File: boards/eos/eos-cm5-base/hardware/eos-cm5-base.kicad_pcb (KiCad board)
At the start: 4 copper layers, 90 x 80 mm, 36 parts, among them J1 CM5 1-100, J2 CM5 101-200, J3 USB-C, J4 USB-A, J5 TRJG0926HENL, J6 microSD, J7 GPIO, J8 FAN, J9 BOOT, SW1 POWER, U1 USBLC6-2SC6, U2 TPS2051C, U3 USBLC6-2SC6, U4 TPD4EUSB30, U5 TPD4EUSB30, U6 RT9742GGJ5

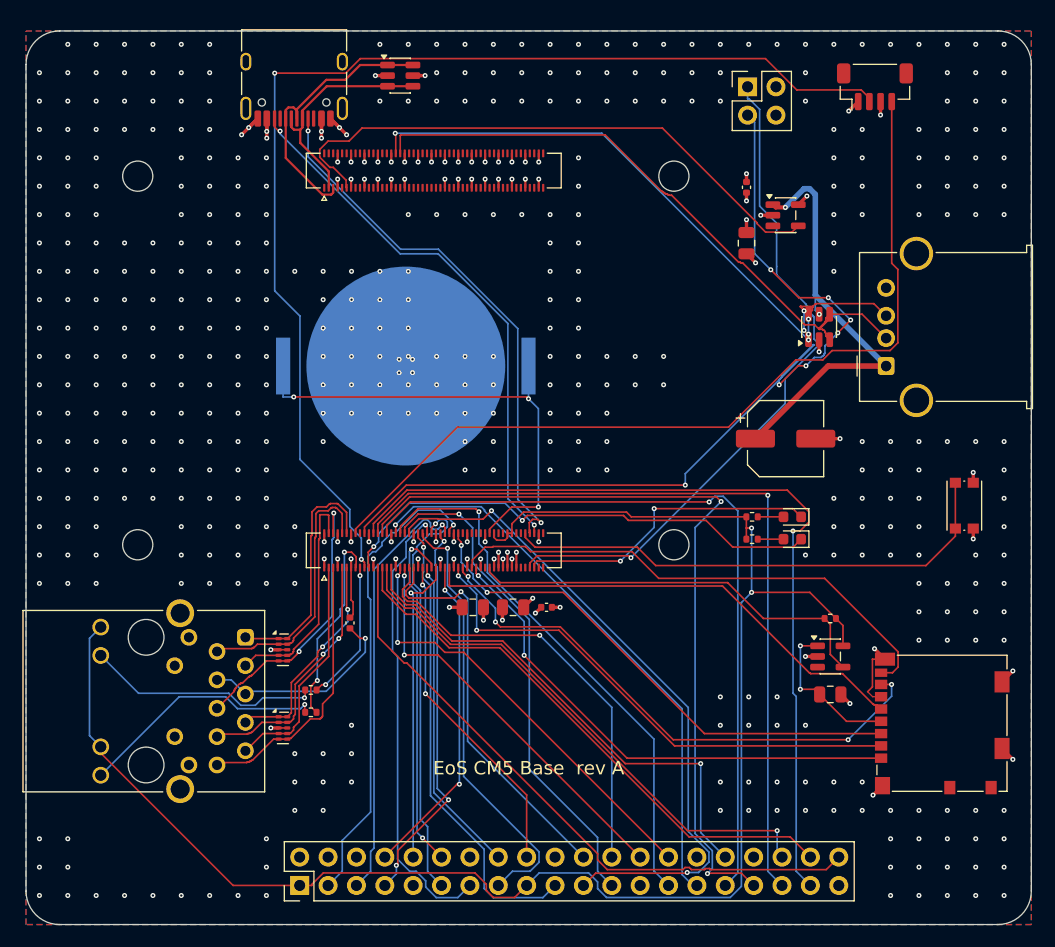
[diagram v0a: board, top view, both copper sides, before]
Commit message: fix(boards): no copper under the CM5's antenna on EoS CM5 Base
The CM5 datasheet (section 4.1.2) says "Don't place any metal, including ground planes,
directly beneath the antenna" and asks for a ground-plane cut-out of at least 6.5 x 11 mm,
ideally 8 x 15 mm. EoS CM5 Base had its ground and 5 V planes and both pours under the whole
module, the antenna included.

- tools/eos_boards gains `copper_keepouts`: rectangles kept free of copper on every layer.
  Each is a rule area on the saved board (no tracks, vias, pads or pours), so zone fills, the
  router's DSN and DRC all honour it. _inside() also refuses them, so the plane fan-out, the
  ground stitching and the maze router never put a via or track there.
- EoS CM5 Base keeps the datasheet's ideal 8 x 15 mm clear where Figure 4 puts the cut-out:
  the module's pin-99 edge, 18.5 mm up from the pin-200 edge. That is x 55-63, y 26-41 mm on
  the board, and nothing is placed there.
- With the planes cut back there, the autorouter boxed SD_DAT0 in and the build stopped at 1
  unconnected item. So SD_DAT1, SD_DAT0 and SD_CLK are now routed first, shortest first, and
  nest on the top layer. Rebuilt: ERC 0, DRC errors 0, unconnected 0, parity 0, 6 silkscreen
  warnings as before.
- AntennaKeepoutTest reads the built board and checks four things:
  - the rule area is there, on every copper layer;
  - it covers Figure 4's cut-out and is at least 8 x 15 mm;
  - no track or via enters it;
  - no pour covers any of 49 points inside it.
  It fails on the previous board (no rule area). It also fails on this board with one track or
  one via added inside, and KiCad's DRC then reports items_not_allowed too.
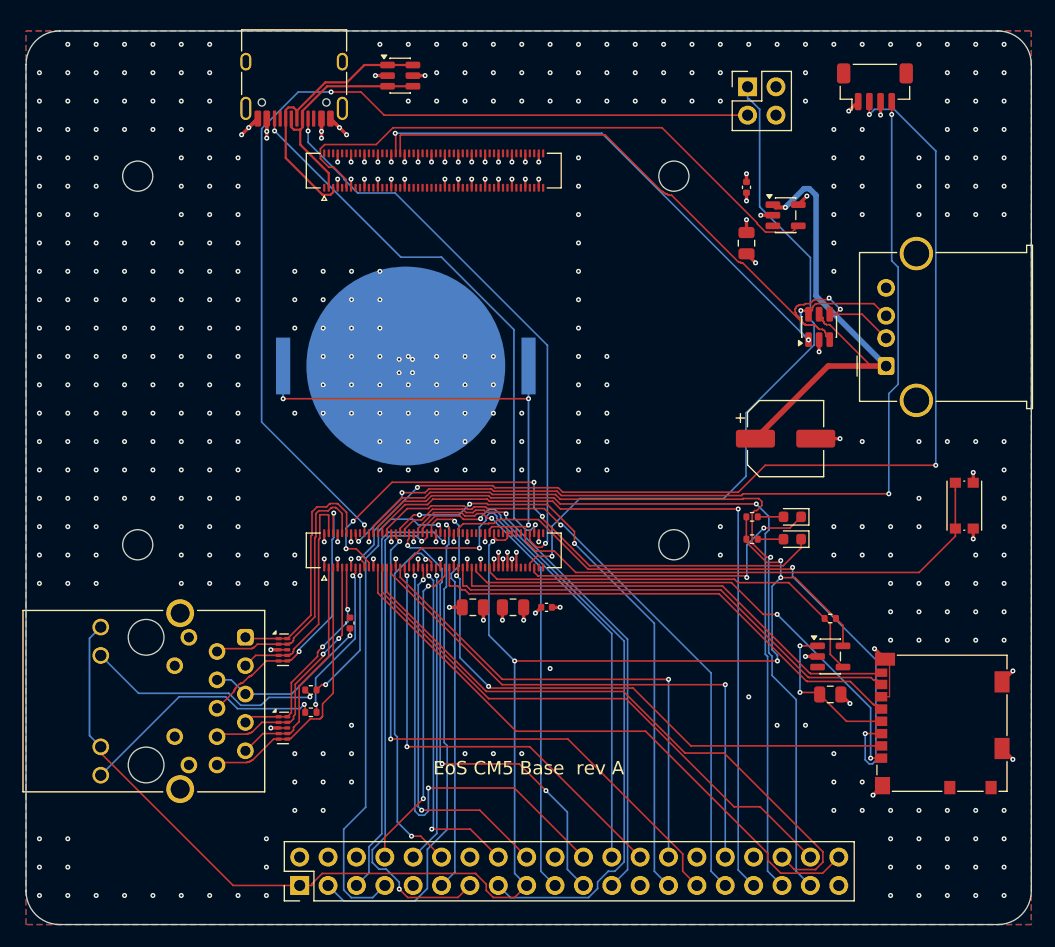
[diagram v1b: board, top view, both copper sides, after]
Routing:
- net /GPIO22: track 39.0 -> 57.7 mm
- net /GPIO9: track 60.1 -> 42.9 mm, vias 2 -> 3
- net /GPIO6: track 67.7 -> 56.2 mm
- net /SD_CMD: track 46.9 -> 57.9 mm
- net /GPIO4: track 34.9 -> 44.7 mm, vias 3 -> 1
- net +3V3: track 149.9 -> 141.0 mm, vias 2 -> 5
- net /FAN_TACHO: track 77.6 -> 86.5 mm, vias 0 -> 4
- net /FAN_PWM: track 103.1 -> 94.4 mm, vias 2 -> 4
- net /LED_NACT: track 44.7 -> 53.3 mm, vias 2 -> 4
- net /GPIO16: track 48.4 -> 56.2 mm, vias 1 -> 0
- net /GPIO8: track 39.1 -> 46.4 mm
- net /SD_DAT0: track 49.6 -> 42.7 mm, vias 4 -> 0
- net /USBH_VBUS: track 39.0 -> 45.3 mm, vias 2 -> 1
- net /USBH_DM: track 56.9 -> 63.1 mm, vias 0 -> 2
- net GND: track 80.9 -> 75.2 mm, vias 499 -> 460
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
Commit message: fix(boards): USB-C receptacles at HRO's recommended edge distance
Each HRO TYPE-C-31-M-12 now sits with its footprint origin 3.19 mm from the
board edge it faces (design.USB_C_EDGE). HRO's "RECOMMEND P.C.B LAYOUT" draws
the PCB edge 5.79 mm from the locating pegs, which are 2.60 mm behind the
origin. At the old 3.8 mm the shell's face was 0.15 mm behind the edge, so a
plug's overmold could meet the board before the plug seated; the shell now
stands about 0.46 mm proud of it.

EoS Learn RP2350, EoS Probe S3 and EoS CM5 Base are moved and rebuilt: all
three report ERC 0, DRC errors 0, unconnected 0, schematic parity 0, with the
same DRC warnings as before (4, 4 and 6). On EoS CM5 Base, GPIO2 (the
header's SDA, CM5 pin 58) is now a priority route: after the move the
autorouter boxed its pad in twice, also with 100 passes.

UsbCEdgeTest checks every board's receptacles against the constant, within
the drawing's 0.05 mm tolerance. It fails for the old 3.8 mm placement.

Found in the independent review of a later board (EoS TM4C123 Board, M1).
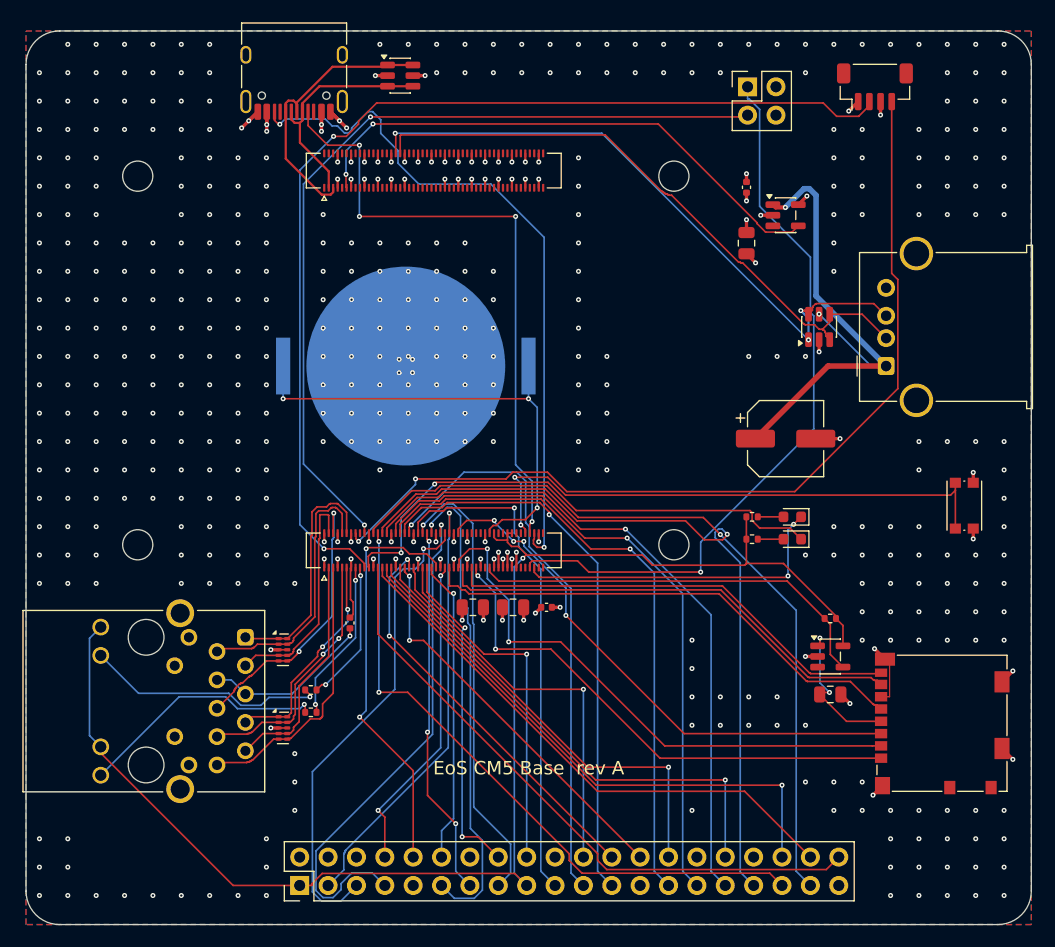
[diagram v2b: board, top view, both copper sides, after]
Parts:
- moved J3 0.61 mm to (24.0, 3.19)
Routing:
- net /GPIO22: track 57.7 -> 41.0 mm
- net /GPIO19: track 71.3 -> 57.9 mm, vias 1 -> 2
- net /CC2: track 50.1 -> 62.5 mm
- net +3V3: track 141.0 -> 128.9 mm, vias 5 -> 1
- net /GPIO27: track 44.8 -> 33.2 mm, vias 2 -> 3
- net /GPIO15: track 26.8 -> 37.1 mm, vias 1 -> 2
- net /GPIO8: track 46.4 -> 36.4 mm, vias 1 -> 2
- net /EEPROM_NWP: track 85.8 -> 75.8 mm
- net /SD_CMD: track 57.9 -> 48.2 mm, vias 2 -> 4
- net /GPIO9: track 42.9 -> 51.7 mm, vias 3 -> 1
- net /USBH_DM: track 63.1 -> 55.5 mm, vias 2 -> 0
- net /LED_NACT: track 53.3 -> 46.9 mm, vias 4 -> 2
- net /GPIO17: track 36.8 -> 43.2 mm
- net /GPIO25: track 41.9 -> 35.8 mm, vias 2 -> 1
- net /GPIO16: track 56.2 -> 50.3 mm, vias 0 -> 1
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
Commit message: fix(boards): rebuild the ten boards made before the no-via-in-pad rule (#55)
PR #64's generator keeps vias out of surface pads (a chip's exposed pad
aside) and 0.1 mm from their own net's pads. Ten boards on master were built
before that rule and had 34 pads with a via in or beside them. They are
rebuilt with the same generator: ATmega328P, RA2E1, KE16Z, KL25, STM32 64,
ESP32 DevKit, Learn RP2350, LPC55S69, CM4 Base and CM5 Base. Each builds at
ERC 0, DRC errors 0, unconnected 0 and parity 0, with the same parts, values,
nets and positions and the same DRC warnings as before.

Where the router could no longer close a short link without a via in a pad,
or left a ground pad without a good path to a via, the design files use
routing options only: priority routes, fanout_first, ground_vias, and a
bottom-layer router keep-out under KL25's crystal (so RESET_b no longer runs
under it). ViaInPadTest drops BUILT_BEFORE_THE_RULE; it now allows only Learn
RP2350's two Raspberry Pi reference vias, named by position. READMEs, TASKS
and CHANGELOG follow the rebuilt copper. Independent verification: three
rounds; the owner adopted a two-layer pour-island criterion (TASKS.md).

Part of #55.
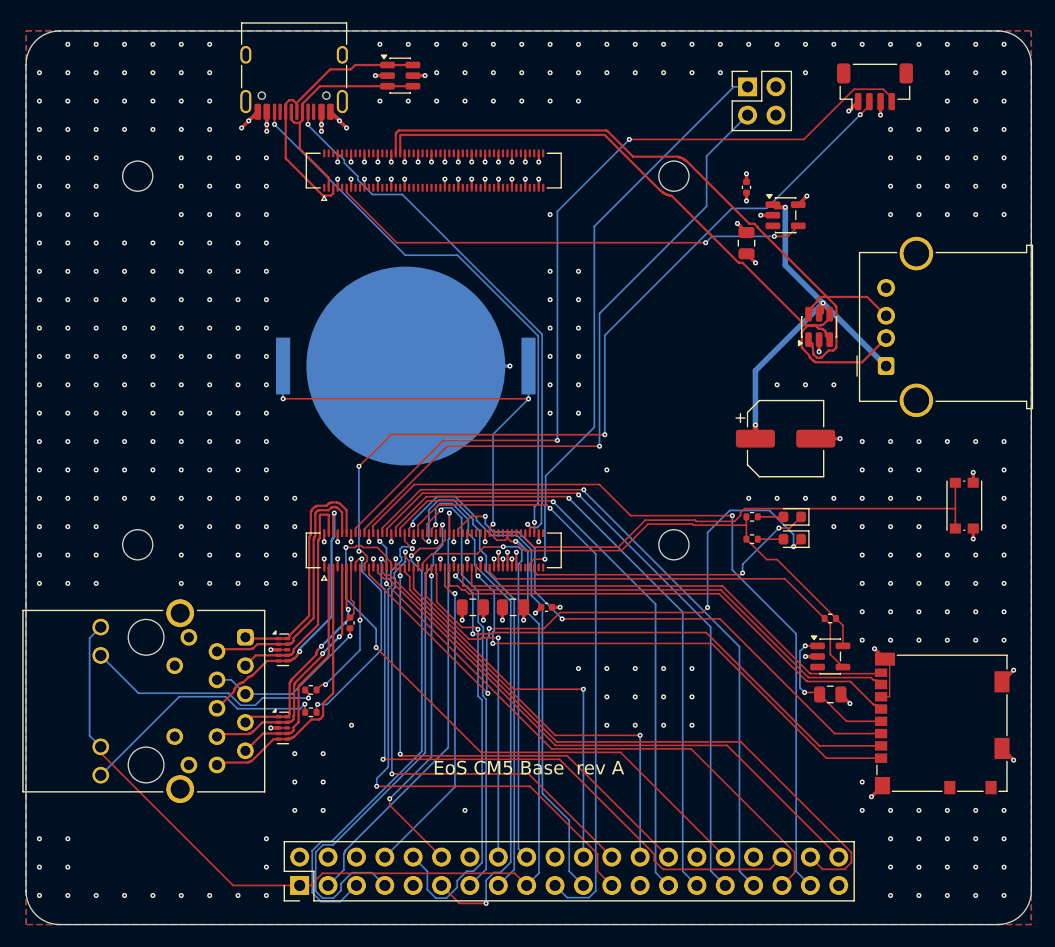
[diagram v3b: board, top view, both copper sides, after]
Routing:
- net /FAN_PWM: track 94.2 -> 74.3 mm, vias 2 -> 4
- net /EEPROM_NWP: track 75.8 -> 59.6 mm, vias 2 -> 1
- net /NRPIBOOT: track 66.4 -> 52.4 mm
- net /LED_NACT: track 46.9 -> 60.1 mm, vias 2 -> 4
- net /CC2: track 62.5 -> 50.4 mm
- net /USBH_VBUS: track 45.1 -> 35.0 mm, vias 2 -> 3
- net /GPIO16: track 50.3 -> 59.8 mm, vias 1 -> 2
- net /GPIO12: track 45.1 -> 54.4 mm, vias 1 -> 2
- net GND: track 79.9 -> 88.8 mm, vias 476 -> 430
- net /GPIO20: track 49.5 -> 58.1 mm
- net /GPIO8: track 36.4 -> 44.7 mm
- net /GPIO10: track 45.4 -> 53.7 mm
- net /GPIO13: track 69.4 -> 61.6 mm
- net /CC1: track 56.0 -> 49.6 mm, vias 4 -> 2
- net /USBH_DM: track 55.5 -> 61.8 mm
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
